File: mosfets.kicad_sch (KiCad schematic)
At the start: 0 parts

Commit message: SCHEMATIC DONE - NEED REVIEW
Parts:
- added C36, C40, C43: 100nf, Capacitor_THT:C_Disc_D10.5mm_W5.0mm_P5.00mm, symbol Device:C
- added C37, C41, C44: 4.7uF, Capacitor_THT:C_Axial_L17.0mm_D7.0mm_P25.00mm_Horizontal, symbol Device:C
- added C38, C39: 10uF, Capacitor_THT:C_Radial_D12.5mm_H25.0mm_P5.00mm, symbol Device:C
- added C42: 10uF, Capacitor_THT:C_Axial_L17.0mm_D7.0mm_P25.00mm_Horizontal, symbol Device:C
- added D4, D5, D6: UF4007, Diode_THT:D_DO-35_SOD27_P7.62mm_Horizontal, symbol Device:D
- added H3: PHASE_A, MountingHole:MountingHole_3.7mm_Pad_Via, symbol Mechanical:MountingHole_Pad
- added H4: PHASE_B, MountingHole:MountingHole_3.7mm_Pad_Via, symbol Mechanical:MountingHole_Pad
- added H5: PHASE_C, MountingHole:MountingHole_3.7mm_Pad_Via, symbol Mechanical:MountingHole_Pad
- added Q10, Q11, Q12, Q13, Q2, Q3, Q4, Q5, Q6, Q7, Q8, Q9: IXTP90N15T, Package_TO_SOT_THT:SIPAK_Vertical, symbol Transistor_FET:IRF4905
- added R20, R21, R22, R23, R32, R33, R34, R35, R42, R43, R44, R45: 22, Resistor_THT:R_Axial_DIN0207_L6.3mm_D2.5mm_P7.62mm_Horizontal, symbol Device:R
- added R24, R25, R30, R31, R40, R41: 100, Resistor_THT:R_Axial_DIN0207_L6.3mm_D2.5mm_P7.62mm_Horizontal, symbol Device:R
- added R26, R27, R28, R29, R36, R37, R38, R39, R46, R47, R48, R49: 10K, Resistor_THT:R_Axial_DIN0207_L6.3mm_D2.5mm_P7.62mm_Horizontal, symbol Device:R
- added U5, U6, U7: IR2110, Package_DIP:DIP-14_W7.62mm, symbol Driver_FET:IR2110
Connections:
- new net: Q4.1 (G), R22.2, R26.1
- new net: H3.1, Q2.3 (S), Q3.2 (D), Q4.3 (S), Q5.2 (D), R26.2, R27.2, U5.5 (VS)
- new net: Q13.1 (G), R42.2, R49.1
- new net: H5.1, Q10.3 (S), Q11.2 (D), Q12.2 (D), Q13.3 (S), R47.2, R49.2, U7.5 (VS)
- new net: R20.1, R21.1, U5.1 (LO)
- new net: R24.2, U5.10 (HIN)
- new net: R25.1, U5.12 (LIN)
- new net: D4.1 (K), U5.6 (VB)
- new net: R22.1, R23.1, U5.7 (HO)
- new net: D6.1 (K), U7.6 (VB)
- new net: C44.1, D6.2 (A)
- new net: Q7.1 (G), R35.2, R36.2
- new net: R41.1, U7.12 (LIN)
- new net: R34.1, R35.1, U6.1 (LO)
- new net: R30.2, U6.10 (HIN)
- new net: R31.1, U6.12 (LIN)
- new net: H4.1, Q6.3 (S), Q7.2 (D), Q8.2 (D), Q9.3 (S), R37.2, R39.2, U6.5 (VS)
- new net: D5.1 (K), U6.6 (VB)
- new net: R32.1, R33.1, U6.7 (HO)
- new net: R44.1, R45.1, U7.1 (LO)
- new net: Q12.1 (G), R44.2, R48.2
- new net: Q10.1 (G), R43.2, R47.1
- new net: Q9.1 (G), R32.2, R39.1
- new net: Q5.1 (G), R21.2, R29.2
- new net: Q3.1 (G), R20.2, R28.2
- new net: Q8.1 (G), R34.2, R38.2
- new net: Q2.1 (G), R23.2, R27.1
- new net: Q6.1 (G), R33.2, R37.1
- new net: R40.2, U7.10 (HIN)
- new net: C41.1, D5.2 (A)
- new net: C37.1, D4.2 (A)
- new net: Q11.1 (G), R45.2, R46.2
- new net: R42.1, R43.1, U7.7 (HO)
- new net +12V: C36.1, C37.2, C38.1, C39.1, C40.1, C41.2, C42.1, C43.1, C44.2, U5.3 (VCC), U6.3 (VCC), U7.3 (VCC)
- new net +3V3: U5.9 (VDD), U6.9 (VDD), U7.9 (VDD)
- new net +VDC: Q10.2 (D), Q13.2 (D), Q2.2 (D), Q4.2 (D), Q6.2 (D), Q9.2 (D)
- new net -VDC: Q11.3 (S), Q12.3 (S), Q3.3 (S), Q5.3 (S), Q7.3 (S), Q8.3 (S), R28.1, R29.1, R36.1, R38.1, R46.1, R48.1
- new net GND: C36.2, C38.2, C39.2, C40.2, C42.2, C43.2, U5.13 (VSS), U5.2 (COM), U6.13 (VSS), U6.2 (COM), U7.13 (VSS), U7.2 (COM)
- new net HS_MOS_A: R24.1
- new net HS_MOS_B: R30.1
- new net HS_MOS_C: R40.1
- new net LS_MOS_A: R25.2
- new net LS_MOS_B: R31.2
- new net LS_MOS_C: R41.2

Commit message: LATEST UPDATES
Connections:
- net -VDC: now also C36.2, C38.2, C39.2, C40.2, C42.2, C43.2, U5.2 (COM), U6.2 (COM), U7.2 (COM)
- net GND: no longer C36.2, C38.2, C39.2, C40.2, C42.2, C43.2, U5.2 (COM), U6.2 (COM), U7.2 (COM)

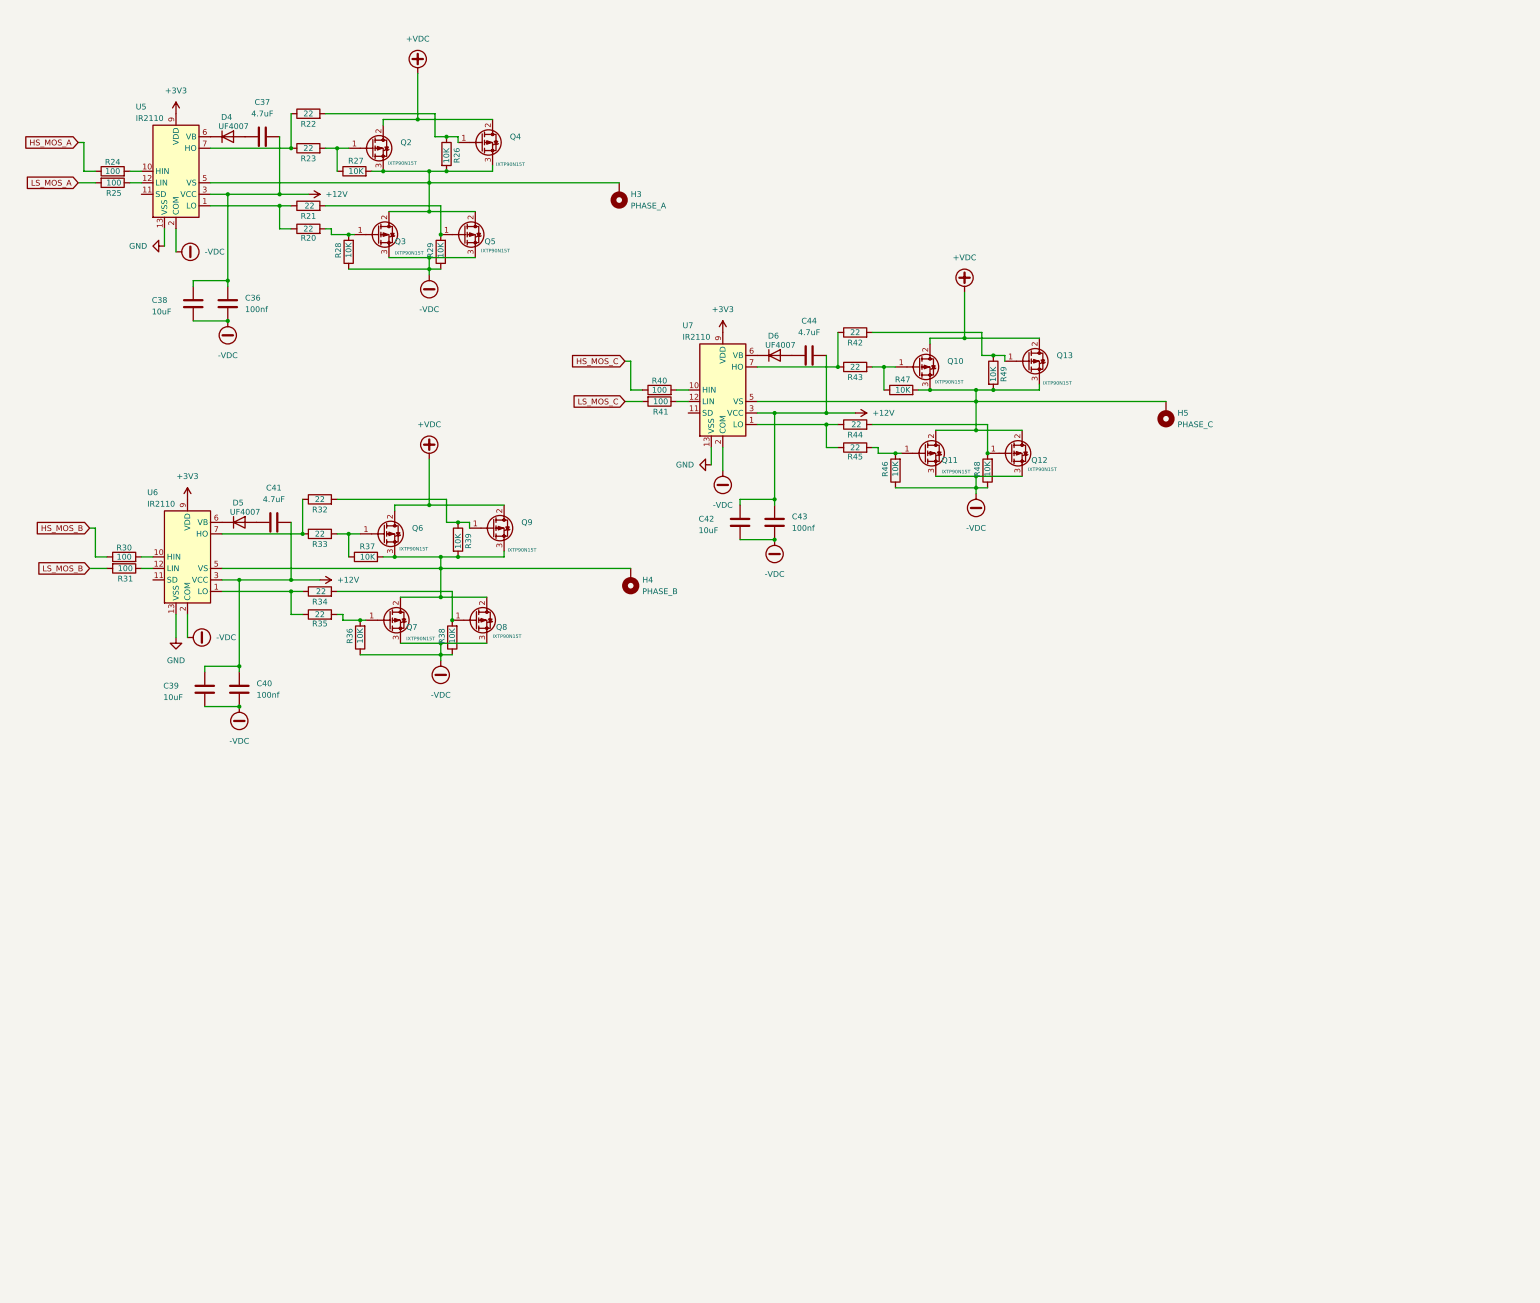
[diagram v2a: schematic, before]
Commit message: Fet Drivers  olarak IRS21867S, MOSFET olarak IAUS300N08S5N014 değiştirildi. Decoupler kısmı değiştirildi, (paraziter direnci arttırıldı.) buzzer düzeltildi ve utility kısmına alındı. CAN-BUS bitti. LDO sayısı 2x oldu
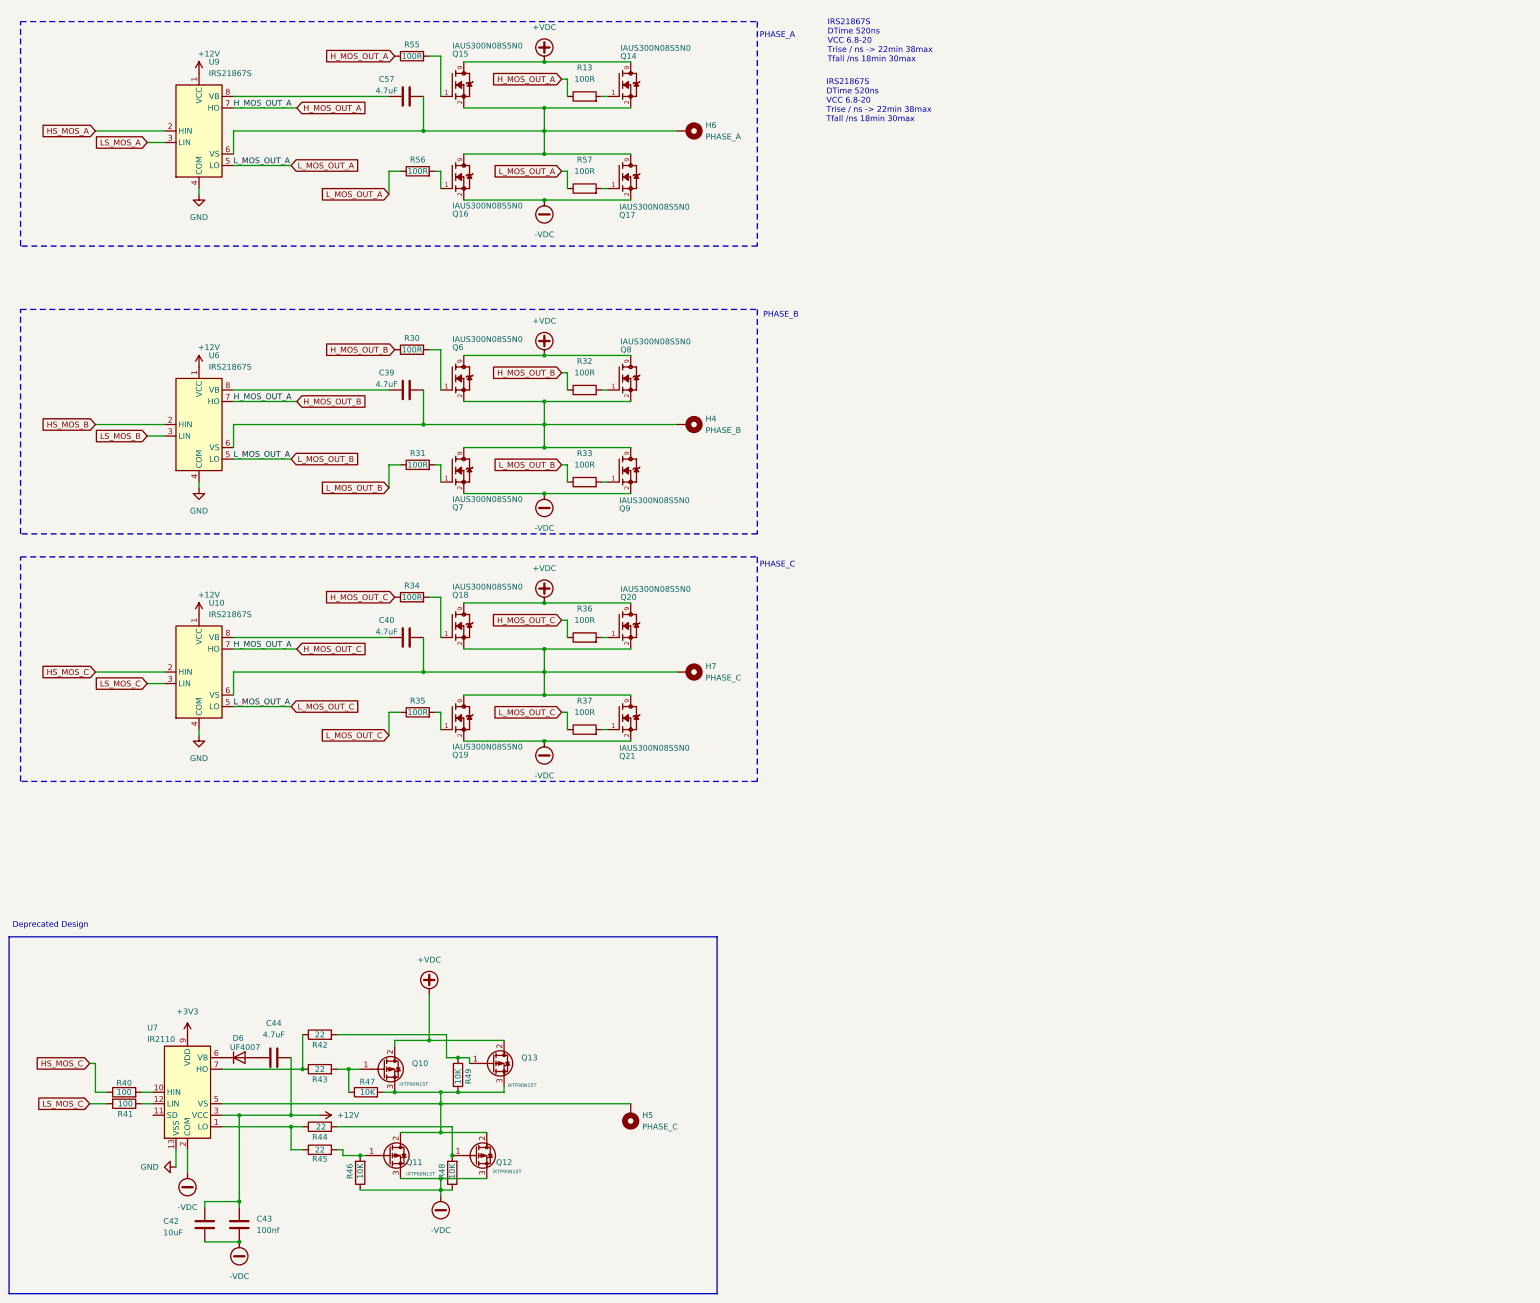
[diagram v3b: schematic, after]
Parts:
- removed C36: 100nf, Capacitor_THT:C_Disc_D10.5mm_W5.0mm_P5.00mm, symbol Device:C
- removed C37, C41: 4.7uF, Capacitor_THT:C_Axial_L17.0mm_D7.0mm_P25.00mm_Horizontal, symbol Device:C
- removed C38: 10uF, Capacitor_THT:C_Radial_D12.5mm_H25.0mm_P5.00mm, symbol Device:C
- removed D4, D5: UF4007, Diode_THT:D_DO-35_SOD27_P7.62mm_Horizontal, symbol Device:D
- removed H3: PHASE_A, MountingHole:MountingHole_3.7mm_Pad_Via, symbol Mechanical:MountingHole_Pad
- removed Q2, Q3, Q4, Q5, Q6, Q7, Q8, Q9: IXTP90N15T, Package_TO_SOT_THT:SIPAK_Vertical, symbol Transistor_FET:IRF4905
- removed R20, R21, R22, R23: 22, Resistor_THT:R_Axial_DIN0207_L6.3mm_D2.5mm_P7.62mm_Horizontal, symbol Device:R
- removed R24, R25: 100, Resistor_THT:R_Axial_DIN0207_L6.3mm_D2.5mm_P7.62mm_Horizontal, symbol Device:R
- removed R26, R27, R28, R29, R38, R39: 10K, Resistor_THT:R_Axial_DIN0207_L6.3mm_D2.5mm_P7.62mm_Horizontal, symbol Device:R
- removed U5, U6: IR2110, Package_DIP:DIP-14_W7.62mm, symbol Driver_FET:IR2110
- added C57: 4.7uF, Capacitor_THT:C_Axial_L17.0mm_D7.0mm_P25.00mm_Horizontal, symbol Device:C
- added H6: PHASE_A, MountingHole:MountingHole_3.7mm_Pad_Via, symbol Mechanical:MountingHole_Pad
- added H7: PHASE_C, MountingHole:MountingHole_3.7mm_Pad_Via, symbol Mechanical:MountingHole_Pad
- added Q14, Q15, Q16, Q17, Q18, Q19, Q20, Q21, Q6, Q7, Q8, Q9: IAUS300N08S5N0, IAUS300N08S5N014ATMA1:TRANS_IAUS300N08S5N014ATMA1, symbol IAUS300N08S5N014ATMA1:IAUS300N08S5N014ATMA1
- added R13, R55, R56, R57: 100R, symbol Device:R
- added U10, U6, U9: IRS21867S, Package_SO:SOIC-8_3.9x4.9mm_P1.27mm, symbol Driver_FET:IRS21867S
- C39: value 10uF -> 4.7uF; footprint Capacitor_THT:C_Radial_D12.5mm_H25.0mm_P5.00mm -> Capacitor_THT:C_Axial_L17.0mm_D7.0mm_P25.00mm_Horizontal
- C40: value 100nf -> 4.7uF; footprint Capacitor_THT:C_Disc_D10.5mm_W5.0mm_P5.00mm -> Capacitor_THT:C_Axial_L17.0mm_D7.0mm_P25.00mm_Horizontal
- R30, R31: value 100 -> 100R; footprint Resistor_THT:R_Axial_DIN0207_L6.3mm_D2.5mm_P7.62mm_Horizontal -> (none)
- R32, R33, R34, R35: value 22 -> 100R; footprint Resistor_THT:R_Axial_DIN0207_L6.3mm_D2.5mm_P7.62mm_Horizontal -> (none)
- R36, R37: value 10K -> 100R; footprint Resistor_THT:R_Axial_DIN0207_L6.3mm_D2.5mm_P7.62mm_Horizontal -> (none)
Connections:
- net +12V: now also U10.1 (VCC), U6.1 (VCC), U9.1 (VCC); no longer C39.1, C40.1
- net +VDC: now also Q14.9, Q15.9, Q18.9, Q20.9, Q6.9, Q8.9
- net -VDC: now also Q16.2, Q16.3, Q16.4, Q16.5, Q16.6, Q16.7, Q16.8, Q17.2, Q17.3, Q17.4, Q17.5, Q17.6, Q17.7, Q17.8, Q19.2, Q19.3, Q19.4, Q19.5, Q19.6, Q19.7, Q19.8, Q21.2, Q21.3, Q21.4, Q21.5, Q21.6, Q21.7, Q21.8, Q7.2, Q7.3, Q7.4, Q7.5, Q7.6, Q7.7, Q7.8, Q9.2, Q9.3, Q9.4, Q9.5, Q9.6, Q9.7, Q9.8; no longer C39.2, C40.2, R36.1
- net GND: now also U10.4 (COM), U6.4 (COM), U9.4 (COM)
- net HS_MOS_A: now also U9.2 (HIN)
- net HS_MOS_B: now also U6.2 (HIN); no longer R30.1
- net HS_MOS_C: now also U10.2 (HIN)
- net LS_MOS_A: now also U9.3 (LIN)
- net LS_MOS_B: now also U6.3 (LIN); no longer R31.2
- net LS_MOS_C: now also U10.3 (LIN)
- net at R35.2: now also Q19.1; no longer R36.2
- net H_MOS_OUT_A: now reaches R34.1
- net H_MOS_OUT_A: now also R30.1, R32.1, R36.1, R13.1, R55.1, U10.7 (HO), U6.7 (HO), U9.7 (HO); no longer R35.1
- net at R30.2: now also Q6.1
- net L_MOS_OUT_A: now reaches R31.1
- net L_MOS_OUT_A: now also R33.1, R35.1, R37.1, R56.1, R57.1, U10.5 (LO), U6.5 (LO), U9.5 (LO)
- net at R37.2: now also Q21.1; no longer H4.1
- net at R32.2: now also Q8.1
- net at R34.2: now also Q18.1
- net at R33.2: now also Q9.1; no longer R37.1
- new net: C40.2, H7.1, Q18.2, Q18.3, Q18.4, Q18.5, Q18.6, Q18.7, Q18.8, Q19.9, Q20.2, Q20.3, Q20.4, Q20.5, Q20.6, Q20.7, Q20.8, Q21.9, U10.6 (VS)
- new net: Q15.1, R55.2
- new net: Q16.1, R56.2
- new net: C57.2, H6.1, Q14.2, Q14.3, Q14.4, Q14.5, Q14.6, Q14.7, Q14.8, Q15.2, Q15.3, Q15.4, Q15.5, Q15.6, Q15.7, Q15.8, Q16.9, Q17.9, U9.6 (VS)
- new net: C39.2, H4.1, Q6.2, Q6.3, Q6.4, Q6.5, Q6.6, Q6.7, Q6.8, Q7.9, Q8.2, Q8.3, Q8.4, Q8.5, Q8.6, Q8.7, Q8.8, Q9.9, U6.6 (VS)
- new net: C57.1, U9.8 (VB)
- new net: Q14.1, R13.2
- new net: C40.1, U10.8 (VB)
- new net: C39.1, U6.8 (VB)
- new net: Q7.1, R31.2
- new net: Q20.1, R36.2
- new net: Q17.1, R57.2
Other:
- note added: "Deprecated Design"
- note added: "IRS21867S DTime 520ns VCC 6.8-20 Trise / ns -> 22min 38max Tfall /ns 18min 30max"
- note added: "PHASE_A"
- note added: "PHASE_B"
- note added: "PHASE_C"
- moved on the sheet: C42, C43, C44, D6, H5, Q10, Q11, Q12, Q13, R40, R41, R42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

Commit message: update Current sense
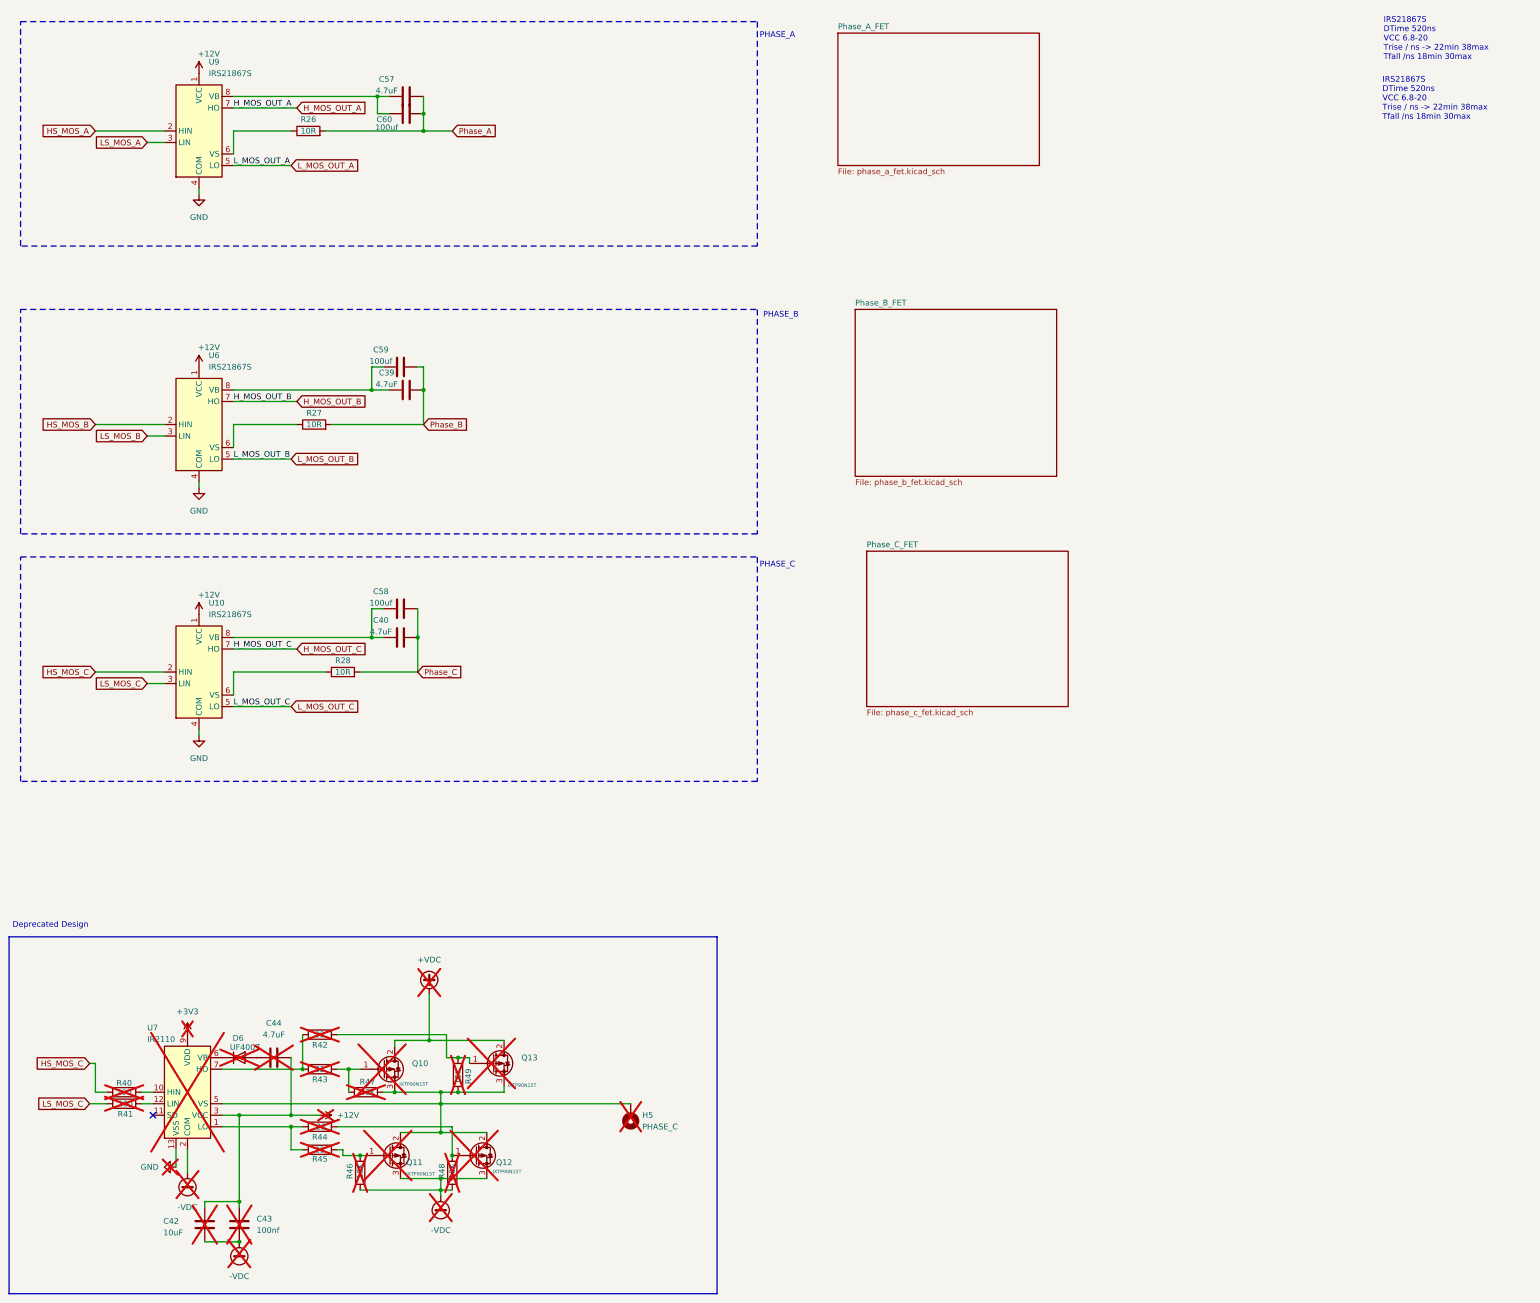
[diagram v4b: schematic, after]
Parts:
- removed H4: PHASE_B, MountingHole:MountingHole_3.7mm_Pad_Via, symbol Mechanical:MountingHole_Pad
- removed H6: PHASE_A, MountingHole:MountingHole_3.7mm_Pad_Via, symbol Mechanical:MountingHole_Pad
- removed H7: PHASE_C, MountingHole:MountingHole_3.7mm_Pad_Via, symbol Mechanical:MountingHole_Pad
- removed Q14, Q15, Q16, Q17, Q18, Q19, Q20, Q21, Q6, Q7, Q8, Q9: IAUS300N08S5N0, IAUS300N08S5N014ATMA1:TRANS_IAUS300N08S5N014ATMA1, symbol IAUS300N08S5N014ATMA1:IAUS300N08S5N014ATMA1
- removed R13, R30, R31, R32, R33, R34, R35, R36, R37, R55, R56, R57: 100R, symbol Device:R
- added C58, C59, C60: 100uf, Capacitor_SMD:C_0805_2012Metric_Pad1.18x1.45mm_HandSolder, symbol Device:C
- added R26, R27, R28: 10R, Resistor_SMD:R_0805_2012Metric_Pad1.20x1.40mm_HandSolder, symbol Device:R
- C39, C40, C57: footprint Capacitor_THT:C_Axial_L17.0mm_D7.0mm_P25.00mm_Horizontal -> Capacitor_THT:C_Rect_L7.2mm_W3.5mm_P5.00mm_FKS2_FKP2_MKS2_MKP2
- C42, C43, C44, D6, Q10, Q11, Q12, Q13, R40, R41, R42, R43, R44, R45, R46, R47, R48, R49, U7: now not fitted; now left out of the parts list
- H5: now not fitted
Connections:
- net H_MOS_OUT_A: no longer U10.7 (HO), U6.7 (HO)
- net L_MOS_OUT_A: no longer U10.5 (LO), U6.5 (LO)
- net at U10.6 (VS): now also R28.1; no longer C40.2
- net at U9.6 (VS): now also R26.1; no longer C57.2
- net at U6.6 (VS): now also R27.1; no longer C39.2
- net at C57.1, U9.8 (VB): now also C60.1
- net at C40.1, U10.8 (VB): now also C58.1
- net at C39.1, U6.8 (VB): now also C59.1
- new net H_MOS_OUT_B: U6.7 (HO)
- new net H_MOS_OUT_C: U10.7 (HO)
- new net L_MOS_OUT_B: U6.5 (LO)
- new net L_MOS_OUT_C: U10.5 (LO)
- new net Phase_A: C57.2, C60.2, R26.2
- new net Phase_B: C39.2, C59.2, R27.2
- new net Phase_C: C40.2, C58.2, R28.2
- no-connect marks 0 -> 1
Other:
- added sheet Phase_A_FET (phase_a_fet.kicad_sch)
- added sheet Phase_B_FET (phase_b_fet.kicad_sch)
- added sheet Phase_C_FET (phase_c_fet.kicad_sch)
- moved on the sheet: C40
